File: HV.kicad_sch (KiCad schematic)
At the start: 30 parts, among them J10 1935161, J6 1935161, J7 Header_Male_Pin_2.54mm_1X3_,_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, J8 RF1-01K-D-00-50-BK-HDW, J9 RF1-01K-D-00-50-BK-HDW, Q1 MCB90N12A-TP, Q2 MCB90N12A-TP, U6 LTV-816S, U8 LTV-816S, U9 MCP6L04T-E/SL

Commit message: update schematique
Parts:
- removed D10: SBRD10200TR, Diodes:DPAK228P1005X240-4N, symbol Diodes:SBRD10200TR
- removed F3: 0697H9120-01, Fuses:TE5_395, symbol Fuses:0697H9120-01
- removed J7: Header_Male_Pin_2.54mm_1X3_,_Unshrouded, Connectors:Headers_2.54mm_1X3, symbol Connectors:Header_Male_Pin_2.54mm_1X3_,_Unshrouded
- removed L1: ATCA-08-471M-H, Inductors:IND_ATCA-08-471M-H, symbol Inductors:ATCA-08-471M-H
- removed Q2: MCB90N12A-TP, IC:MCB90N12ATP, symbol Transistors:MCB90N12A-TP
- removed R21: RC0805JR-072K2L, Resistors:R0805, symbol Resistors:RC0805JR-072K2L
- removed R24: RC0805FR-075K6L, Resistors:R0805, symbol Resistors:RC0805FR-075K6L
- removed R26: RC0805JR-07330RL, Resistors:R0805, symbol Resistors:RC0805JR-07330RL
- removed R29: RMCF0805FT10M0, Resistors:R0805, symbol Resistors:RMCF0805FT10M0
- removed TP10: Test_Point_THM, Connectors:Keystone_5001, symbol Connectors:Test_Point_THM
- removed U8: LTV-816S, IC:4-SMD, symbol Isolators:LTV-816S
- removed unit 1 of U9
- removed unit 3 of U9
- added C402, C404: 885012207103, Capacitors:C0805, symbol Capacitors:885012207103
- added C403: 885012207098, Capacitors:C0805, symbol Capacitors:885012207098
- added R409: RMCF0805FT10M0, Resistors:R0805, symbol Resistors:RMCF0805FT10M0
- added unit 1 of U403
- added unit 3 of U403
- gave numbers to parts that had none: 1
- renumbered C23 to C401, J10 to J401, J6 to J402, J8 to J403, J9 to J404, Q1 to Q401, R22 to R401, R20 to R402, R25 to R403, R27 to R404, R33 to R405, R31 to R406, R28 to R407, R34 to R408, R32 to R410, R30 to R411, U6 to U401, U9 to U403
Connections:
- net ext_HV is gone; now on net HV: J402.2
- net 3.3VA: now also C402.2
- net 5VA: now also C403.2, C404.2, U403.4
- net GNDA: now also C402.1, C403.1, C404.1, U403.11
- net V_amp: now also U403.8
- net e-: now also R409.2
- net at R406.1: now also U403.1, U403.2
- net at R405.1, R406.2: now also U403.10
- net at R411.2, U403.5: now also R409.1
- net at R404.1, R407.2: now also U403.3
- net at R408.1, R410.2: now also U403.9
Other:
- note added: "TODO: AJOUTER ADC SPI + ISOLATION"
- note removed: "TODO: Ajouter condo entrée"
- note removed: "TODO: Ajouter condo sortie"
- note removed: "TODO: Ajouter current sense"
- note removed: "TODO: Vérifier specs"
- title: HV -> HV Sense
- moved on the sheet: C401, J401, J402, J403, J404, Q401, R401, R402, R403, R404, R405, R406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

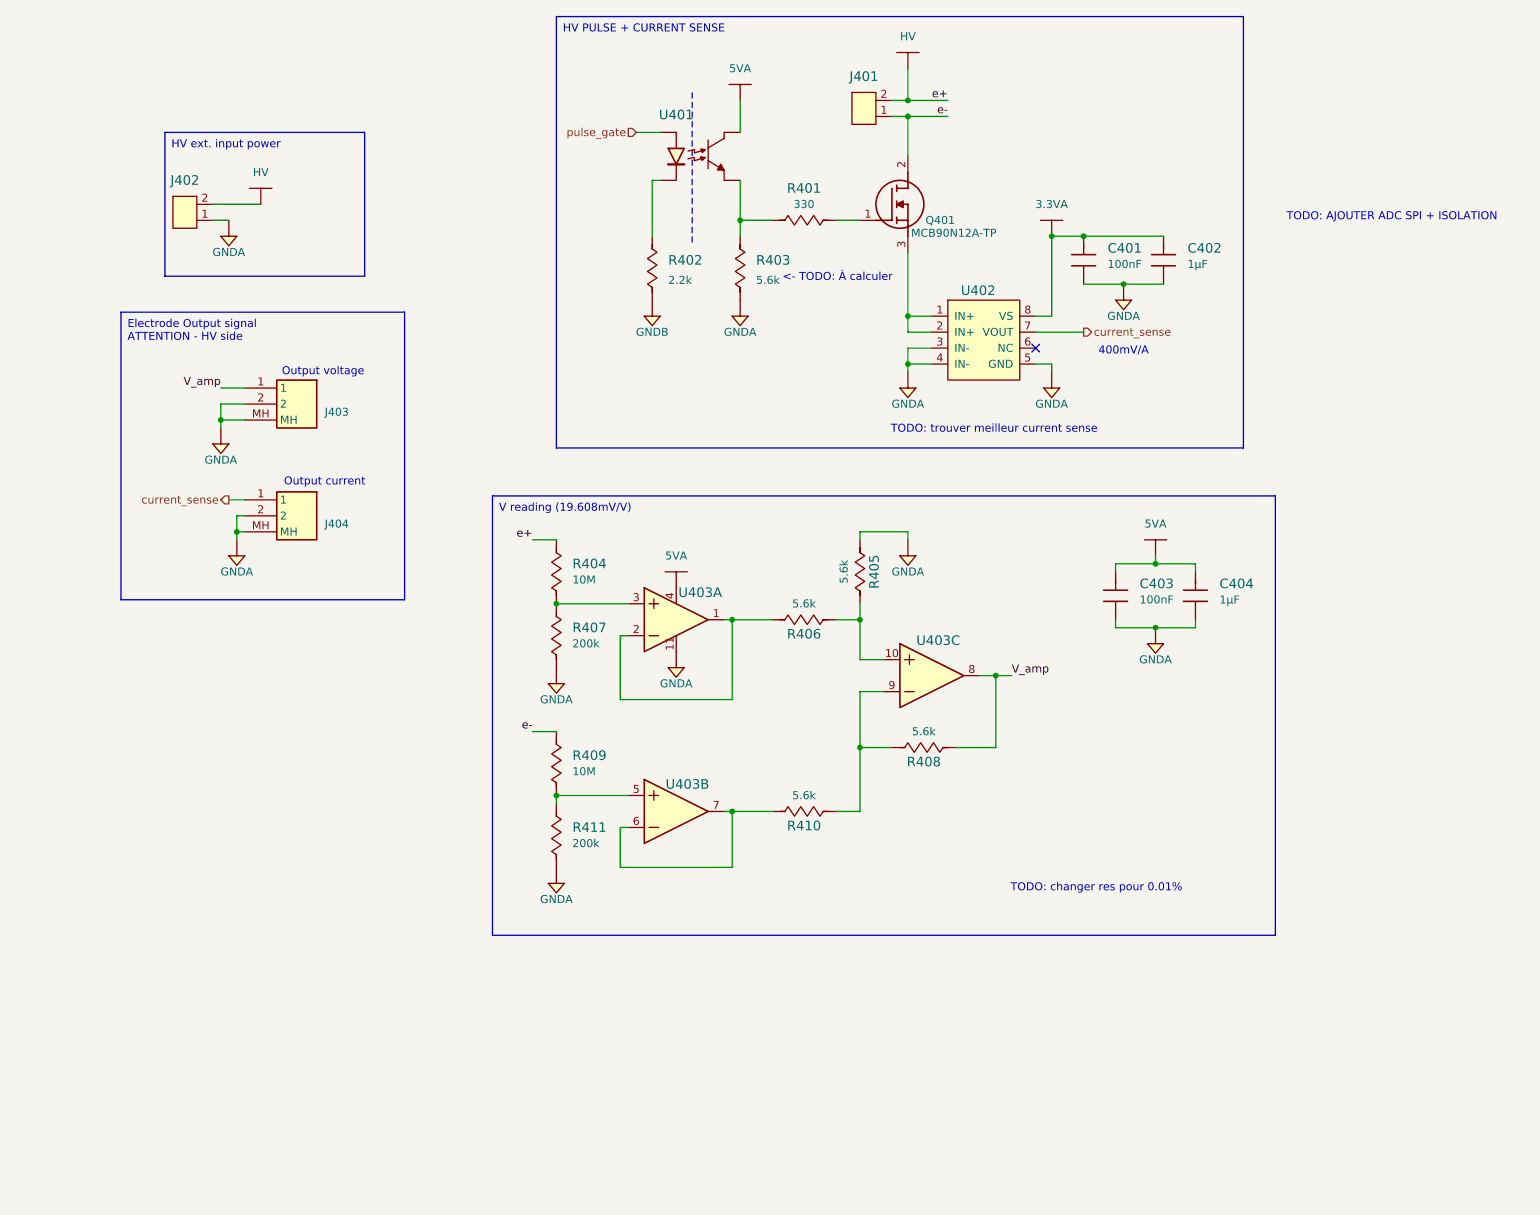
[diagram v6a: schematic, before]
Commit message: update schematic
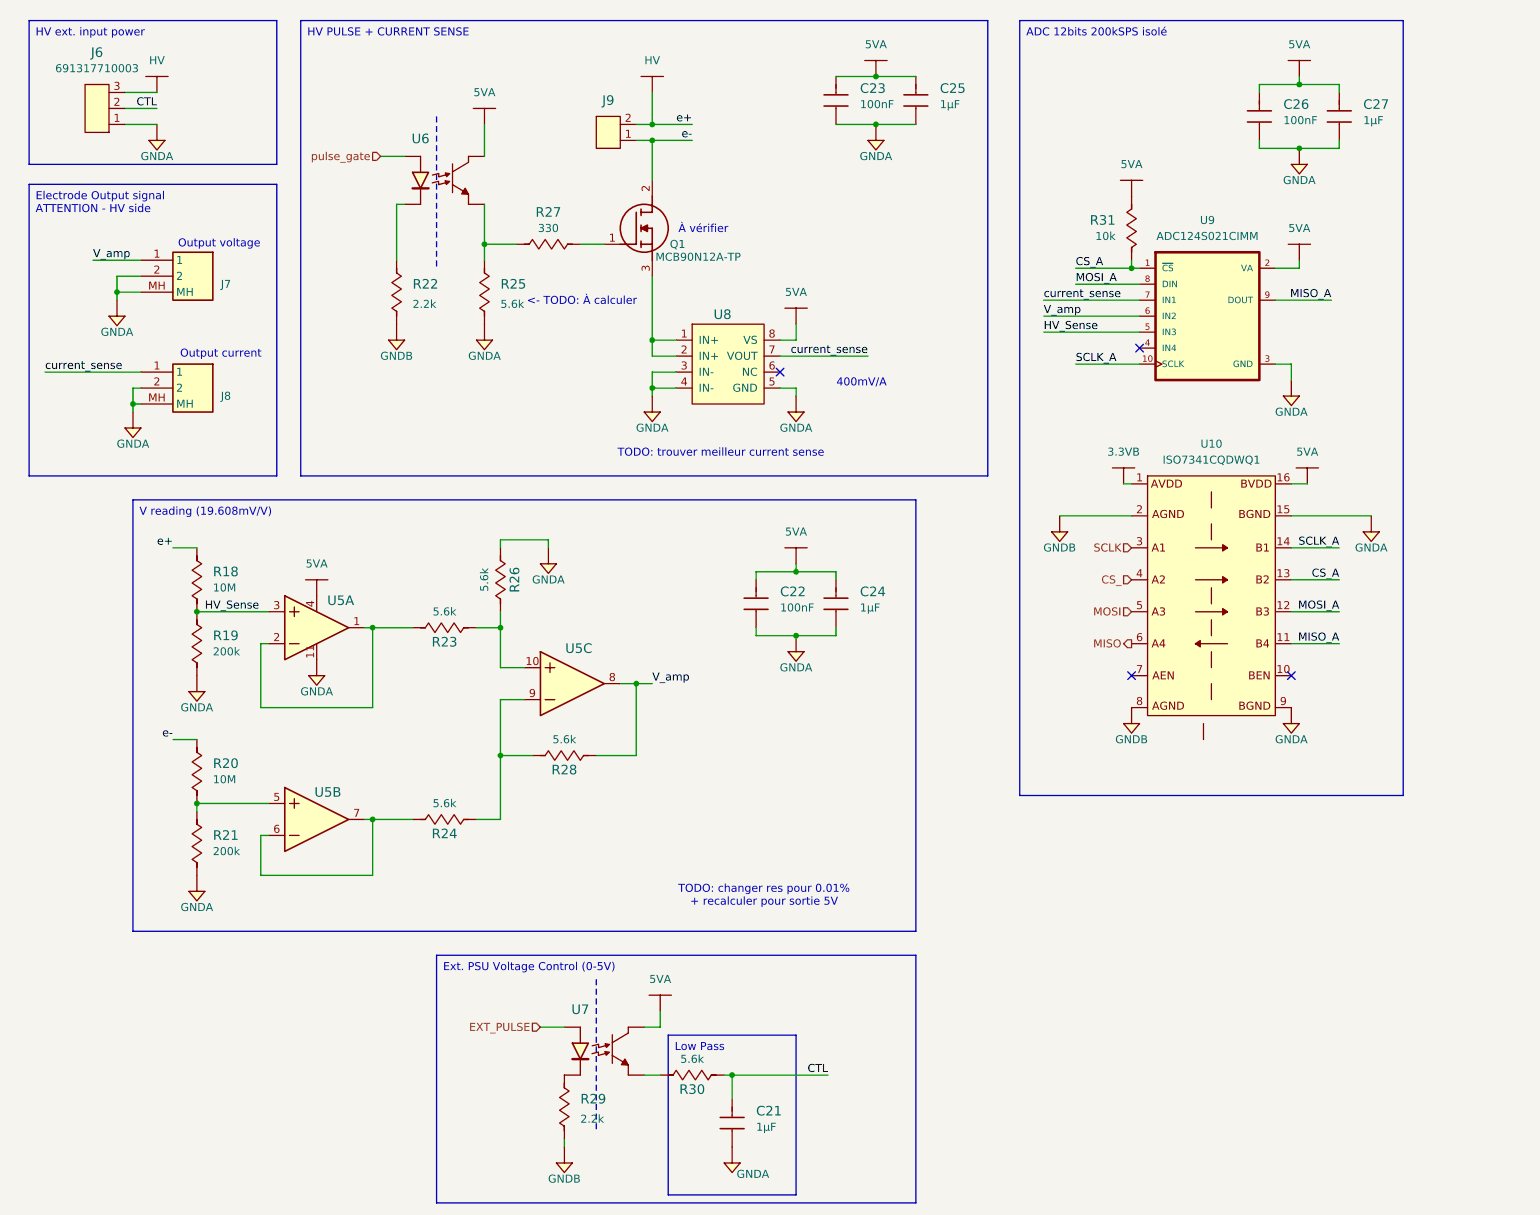
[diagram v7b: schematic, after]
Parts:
- added C21, C27: 885012207103, Capacitors:C0805, symbol Capacitors:885012207103
- added C26: 885012207098, Capacitors:C0805, symbol Capacitors:885012207098
- added R29: RC0805JR-072K2L, Resistors:R0805, symbol Resistors:RC0805JR-072K2L
- added R30: RC0805FR-075K6L, Resistors:R0805, symbol Resistors:RC0805FR-075K6L
- added R31: RC0805JR-0710KL, Resistors:R0805, symbol Resistors:RC0805JR-0710KL
- added U10: ISO7341CQDWQ1, IC:SOIC-16-wide, symbol Isolators:ISO7341CQDWQ1
- added U7: LTV-816S, IC:4-SMD, symbol Isolators:LTV-816S
- added U9: ADC124S021CIMM, IC:SOP50P490X110-10N, symbol ADC:ADC124S021CIMM
- J6: renamed from J402; value 1935161 -> 691317710003; footprint Connectors:1935161 -> Connectors:691317710003; symbol Connectors:1935161 -> Connectors:691317710003; Manufacturer Phoenix Contact -> Wurth Elektronik; Manufacturer Part Number 1935161 -> 691317710003; Supplier Digikey -> Wurth Elektronik; Supplier Part Number 277-1667-ND -> 691317710003
- renumbered C403 to C22, C401 to C23, C404 to C24, C402 to C25, J403 to J7, J404 to J8, J401 to J9, Q401 to Q1, R404 to R18, R407 to R19, R409 to R20, R411 to R21, R402 to R22, R406 to R23, R410 to R24, R403 to R25, R405 to R26, R401 to R27, R408 to R28, U403 to U5, U401 to U6, U402 to U8
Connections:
- net 3.3VA is gone; now on net 5VA: C23.2, C25.2, U8.8 (VS)
- net 5VA: now also C26.2, C27.2, R31.1, U10.16 (BVDD), U7.4 (C), U9.2 (VA)
- net GNDA: now also C21.1, C26.1, C27.1, U10.15 (BGND), U10.9 (BGND), U9.3 (GND)
- net GNDB: now also R29.1, U10.2 (AGND), U10.8 (AGND)
- net HV: now also J6.3; no longer J6.2
- net V_amp: now also U9.6 (IN2)
- net current_sense: now also U9.7 (IN1)
- net HV_Sense: now reaches R18.1, R19.2, U5.3
- net HV_Sense: now also U9.5 (IN3)
- new net: R30.1, U7.3 (E)
- new net: R29.2, U7.2 (Cathode)
- new net 3.3VB: U10.1 (AVDD)
- new net CS_: U10.4 (A2)
- new net CS_A: R31.2, U10.13 (B2), U9.1 (~{CS})
- new net CTL: C21.2, J6.2, R30.2
- new net EXT_PULSE: U7.1 (Anode)
- new net MISO: U10.6 (A4)
- new net MISO_A: U10.11 (B4), U9.9 (DOUT)
- new net MOSI: U10.5 (A3)
- new net MOSI_A: U10.12 (B3), U9.8 (DIN)
- new net SCLK: U10.3 (A1)
- new net SCLK_A: U10.14 (B1), U9.10 (SCLK)
- no-connect marks 1 -> 4
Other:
- note added: "TODO: changer res pour 0.01% + recalculer pour sortie 5V"
- note added: "À vérifier"
- note removed: "TODO: AJOUTER ADC SPI + ISOLATION"
- note removed: "TODO: changer res pour 0.01%"
- moved on the sheet: C22, C23, C24, C25, J7, J8, J9, Q1, R18, R19, R20, R21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

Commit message: finalisation de la schématique
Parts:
- removed C21: 885012207103, Capacitors:C0805, symbol Capacitors:885012207103
- removed J6: 691317710003, Connectors:691317710003, symbol Connectors:691317710003
- removed R18, R20: RMCF0805FT10M0, Resistors:R0805, symbol Resistors:RMCF0805FT10M0
- removed R19, R21: RC0805FR-07200KL, Resistors:R0805, symbol Resistors:RC0805FR-07200KL
- removed R23, R24, R26, R28, R30: RC0805FR-075K6L, Resistors:R0805, symbol Resistors:RC0805FR-075K6L
- removed R29: RC0805JR-072K2L, Resistors:R0805, symbol Resistors:RC0805JR-072K2L
- removed U7: LTV-816S, IC:4-SMD, symbol Isolators:LTV-816S
- added F401: 0698Q6300-01, Fuses:TE5_395, symbol Fuses:0698Q6300-01
- added J401: 1935161, Connectors:1935161, symbol Connectors:1935161
- added R405, R410: ERJ-6ENF1404V, Resistors:R0805, symbol Resistors:ERJ-6ENF1404V
- added R406, R407, R409, R411: RC0805JR-0710KL, Resistors:R0805, symbol Resistors:RC0805JR-0710KL
- added R408, R412: RC0805FR-0747KL, Resistors:R0805, symbol Resistors:RC0805FR-0747KL
- renumbered C23 to C401, C25 to C402, C26 to C403, C27 to C404, C22 to C405, C24 to C406, J9 to J402, J7 to J403, J8 to J404, Q1 to Q401, R31 to R401, R27 to R402, R22 to R403, R25 to R404, U6 to U401, U9 to U402, U8 to U403, U10 to U404, U5 to U405
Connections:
- net GNDA: now also J401.1, R406.1, R408.1, R412.1
- net HV: now also J401.2, R405.2
- net HV_Sense: now also R405.1, R408.2
- net V_amp: now also R409.2
- net e-: now also F401.2, R410.2; no longer Q401.2 (D)
- net at U405.1, U405.2: now also R407.1
- net at U405.10: now also R406.2, R407.2
- net at U405.5: now also R410.1, R412.2
- net at U405.6, U405.7: now also R411.1
- net at U405.9: now also R409.1, R411.2
- net 3.3VB renamed VDD
- new net: F401.1, Q401.2 (D)
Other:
- note removed: "<- TODO: À calculer"
- note removed: "TODO: changer res pour 0.01% + recalculer pour sortie 5V"
- note removed: "TODO: trouver meilleur current sense"
- note removed: "À vérifier"
- moved on the sheet: C405, C406, J402, U405A, U405B, U405C
